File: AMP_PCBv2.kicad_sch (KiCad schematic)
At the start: 37 parts, among them J1 POWER, J2 EBRAKE, J3 MC, J4 STEERING, U1 Teensy4.0, U2 Adafruit_Feather_M0_RFM9x_LoR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, U2 Logo

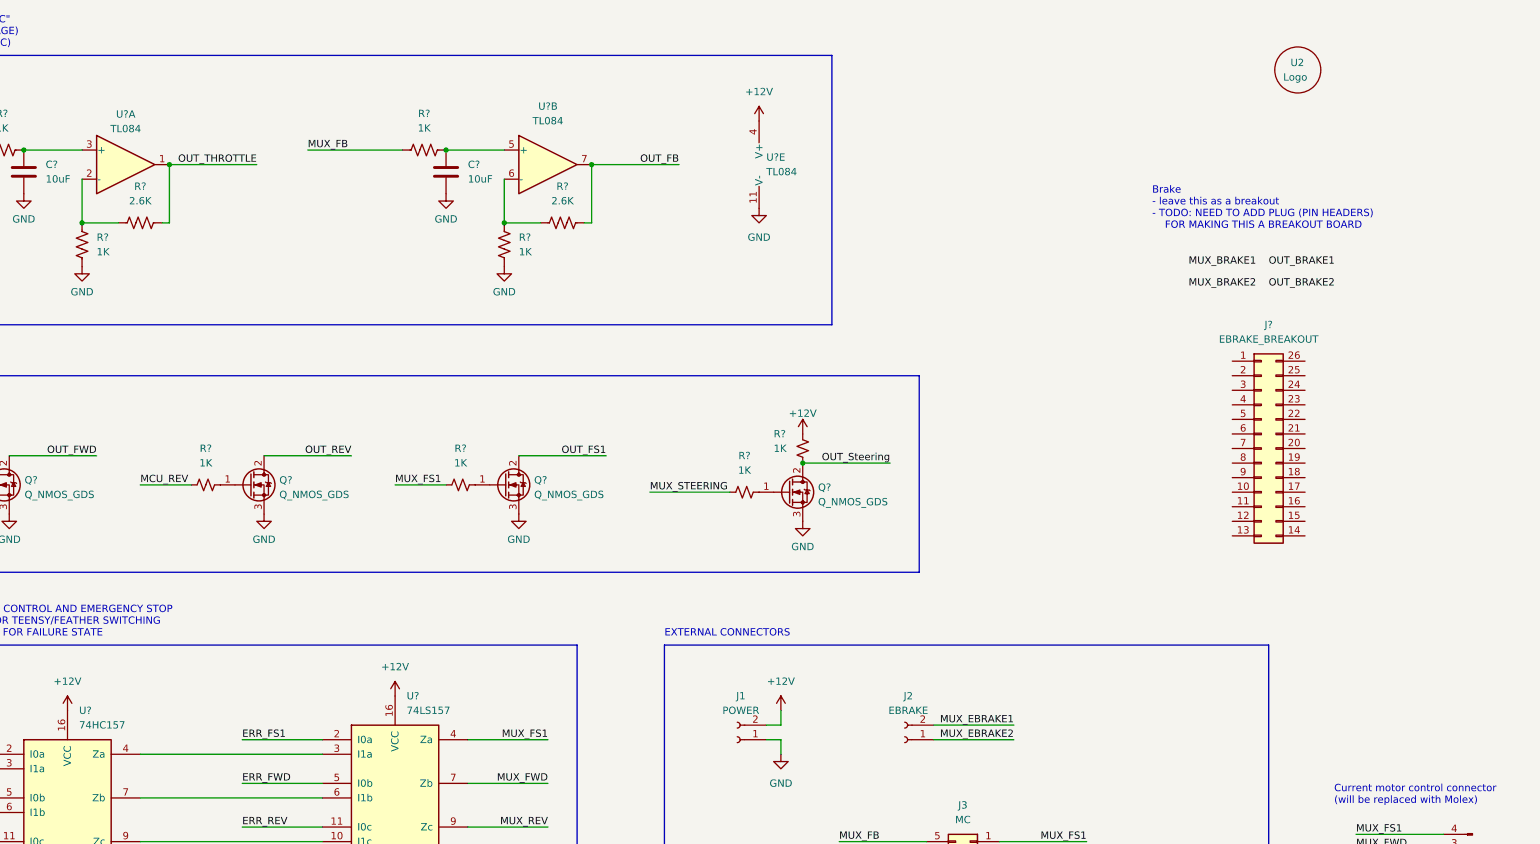
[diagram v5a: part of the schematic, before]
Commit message: Update op-amp PN and add e-brake breakout
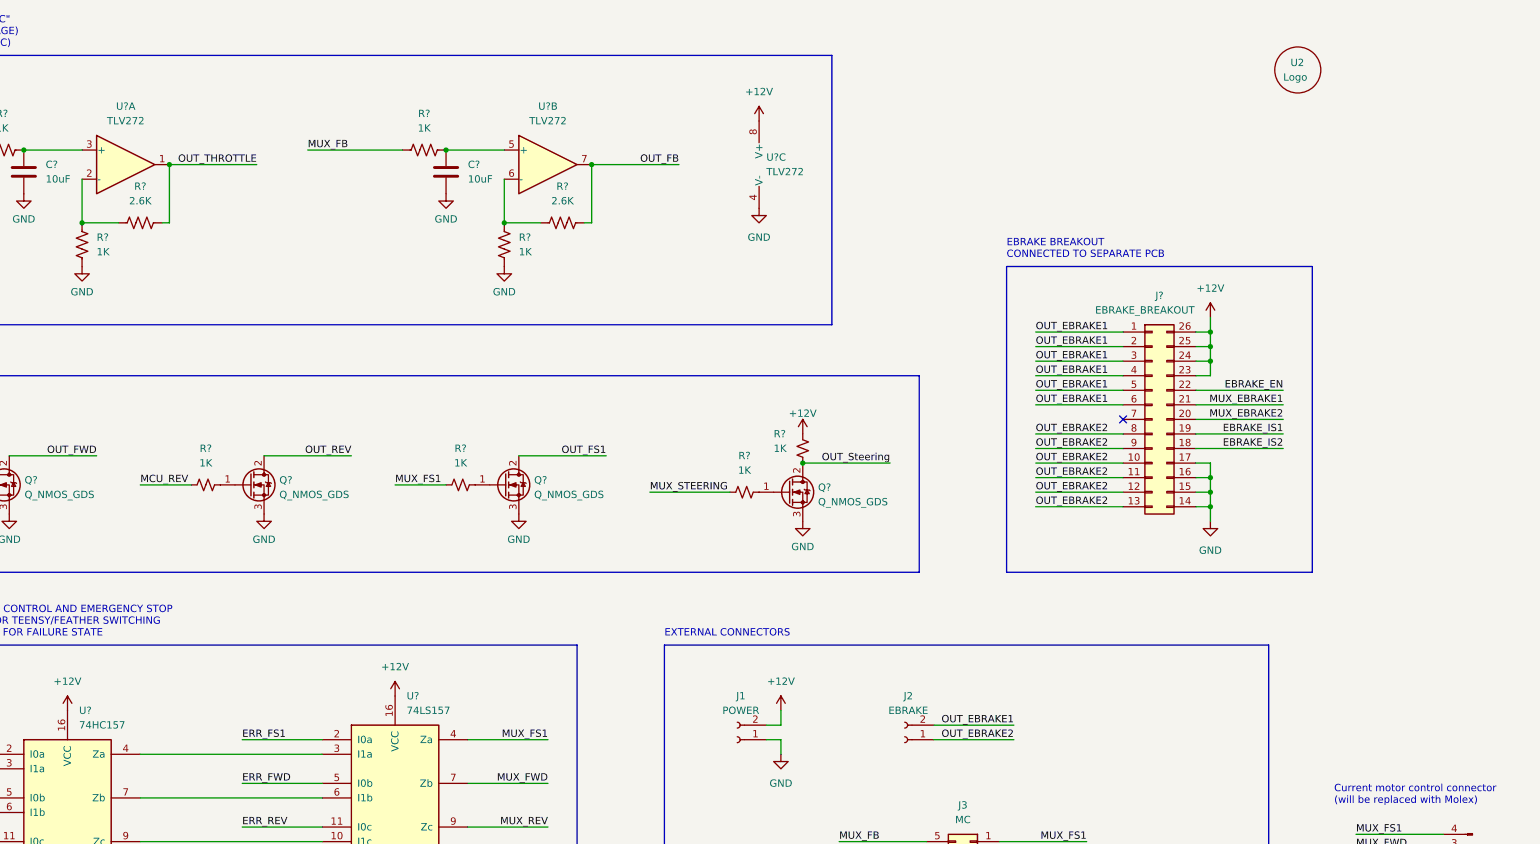
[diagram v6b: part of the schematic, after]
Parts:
- removed U? (x2): TL084, symbol Amplifier_Operational:TL084
- removed U?: TL084, Package_DIP:DIP-14_W7.62mm, symbol Amplifier_Operational:TL084
- added U? (x3): TLV272, symbol Amplifier_Operational:TLV2372
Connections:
- net +12V: now also J?.23 (Pin_23), J?.24 (Pin_24), J?.25 (Pin_25), J?.26 (Pin_26), U?.8 (V+)
- net GND: now also J?.14 (Pin_14), J?.15 (Pin_15), J?.16 (Pin_16), J?.17 (Pin_17), U?.4 (V-)
- net MUX_EBRAKE1: now also J?.21 (Pin_21); no longer J2.2 (Pin_2)
- net MUX_EBRAKE2: now also J?.20 (Pin_20); no longer J2.1 (Pin_1)
- net OUT_FB: now also U?.7
- net OUT_THROTTLE: now also U?.1
- net at R?.1, R?.1: now also U?.6 (-)
- net at R?.1, R?.1: now also U?.2 (-)
- net at C?.1, R?.2: now also U?.3 (+)
- net at C?.1, R?.2: now also U?.5 (+)
- net OUT_EBRAKE1: now reaches J?.1 (Pin_1)
- net OUT_EBRAKE1: now also J2.2 (Pin_2), J?.2 (Pin_2), J?.3 (Pin_3), J?.4 (Pin_4), J?.5 (Pin_5), J?.6 (Pin_6)
- net OUT_EBRAKE2: now reaches J?.10 (Pin_10)
- net OUT_EBRAKE2: now also J2.1 (Pin_1), J?.11 (Pin_11), J?.12 (Pin_12), J?.13 (Pin_13), J?.8 (Pin_8), J?.9 (Pin_9)
- net EBRAKE_IS2: now reaches J?.18 (Pin_18)
- net EBRAKE_IS1: now reaches J?.19 (Pin_19)
- net EBRAKE_EN: now reaches J?.22 (Pin_22)
- no-connect marks 3 -> 4
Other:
- note added: "EBRAKE BREAKOUT CONNECTED TO SEPARATE PCB"
- note removed: "Brake - leave this as a breakout - TODO: NEED TO ADD PLUG (PIN HEADERS) FOR MAKING THIS A BREAKOUT BOARD"
- moved on the sheet: J?

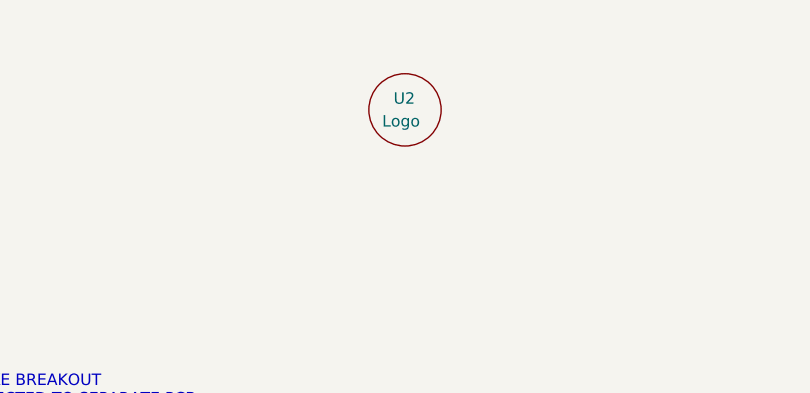
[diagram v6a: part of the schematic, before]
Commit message: Remove logo schematic designator
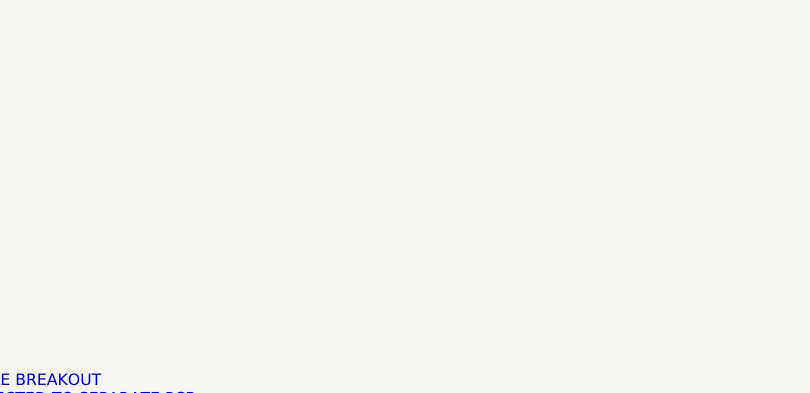
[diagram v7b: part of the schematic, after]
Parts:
- removed U2: Logo, AMP:Logo, symbol AMP:Logo
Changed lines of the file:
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@@
     (pin "1")
-  )
-  (symbol (lib_id "AMP:Logo") (at 361.95 26.67 0) (unit 1)
-    (in_bom no) (on_board yes)
-    (property "Reference" "U2" (id 0) (at 360.68 25.4 0)
-      (effects (font (size 1.27 1.27)) (justify left))
-    )
-    (property "Value" "Logo" (id 1) (at 359.41 27.94 0)
-      (effects (font (size 1.27 1.27)) (justify left))
-    )
-    (property "Footprint" "AMP:Logo" (id 2) (at 361.95 26.67 0)
-      (effects (font (size 1.27 1.27)) hide)
-    )
-    (property "Datasheet" "" (id 3) (at 361.95 26.67 0)
-      (effects (font (size 1.27 1.27)) hide)
-    )
   )
   (symbol (lib_id "power:GND") (at 191.77 245.11 0) (unit 1)
@@
       (reference "U1") (unit 1) (value "Teensy4.0") (footprint "teensy:Teensy40")
     )
-    (path "/83d62449-4592-47d6-9b07-6cbdf8842ef4"
-      (reference "U2") (unit 1) (value "Logo") (footprint "AMP:Logo")
-    )
     (path "/95fe3d96-e8a5-4077-a1d2-b0c02a43836e"

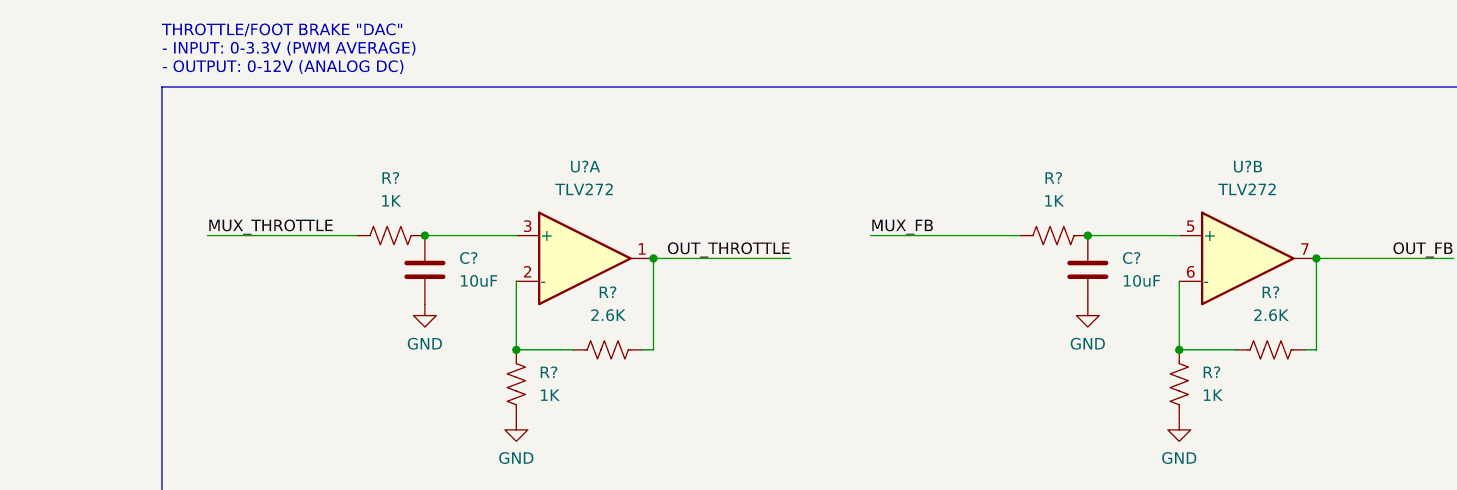
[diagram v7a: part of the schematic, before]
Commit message: Change DAC op-amp gain
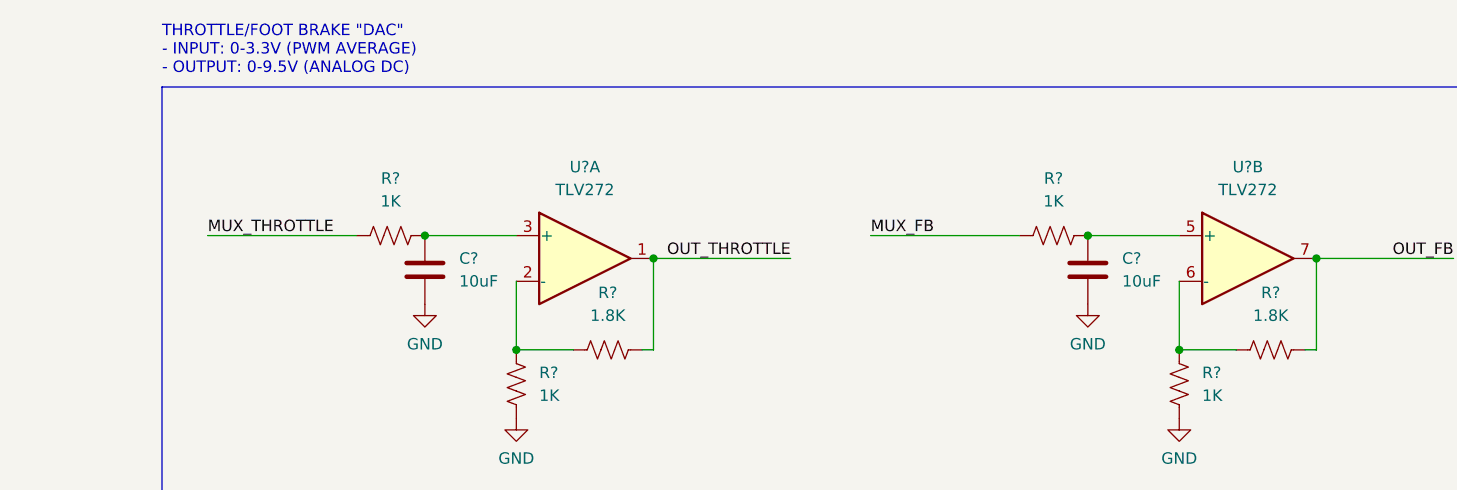
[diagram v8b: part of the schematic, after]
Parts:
- R? (x2): value 2.6K -> 1.8K
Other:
- note added: "THROTTLE/FOOT BRAKE "DAC" - INPUT: 0-3.3V (PWM AVERAGE) - OUTPUT: 0-9.5V (ANALOG DC)"
- note removed: "THROTTLE/FOOT BRAKE "DAC" - INPUT: 0-3.3V (PWM AVERAGE) - OUTPUT: 0-12V (ANALOG DC)"
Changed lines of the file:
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@@
     (effects (font (size 1.27 1.27)) (justify left bottom))
   )
-  (text "THROTTLE/FOOT BRAKE \"DAC\"\n- INPUT: 0-3.3V (PWM AVERAGE)\n- OUTPUT: 0-12V (ANALOG DC)"
+  (text "THROTTLE/FOOT BRAKE \"DAC\"\n- INPUT: 0-3.3V (PWM AVERAGE)\n- OUTPUT: 0-9.5V (ANALOG DC)"
     (at 110.49 22.86 0)
     (effects (font (size 1.27 1.27)) (justify left bottom))
@@
     (in_bom yes) (on_board yes) (fields_autoplaced)
     (property "Reference" "R?" (id 0) (at 233.68 46.99 90))
-    (property "Value" "2.6K" (id 1) (at 233.68 49.53 90))
+    (property "Value" "1.8K" (id 1) (at 233.68 49.53 90))
     (property "Footprint" "" (id 2) (at 233.934 52.324 90)
       (effects (font (size 1.27 1.27)) hide)
@@
     (in_bom yes) (on_board yes) (fields_autoplaced)
     (property "Reference" "R?" (id 0) (at 160.02 46.99 90))
-    (property "Value" "2.6K" (id 1) (at 160.02 49.53 90))
+    (property "Value" "1.8K" (id 1) (at 160.02 49.53 90))
     (property "Footprint" "" (id 2) (at 160.274 52.324 90)
       (effects (font (size 1.27 1.27)) hide)
@@
     )
     (path "/0984d1a3-dac9-4895-b89c-945999a5a91c"
-      (reference "R?") (unit 1) (value "2.6K") (footprint "")
+      (reference "R?") (unit 1) (value "1.8K") (footprint "")
     )
     (path "/2f8c9adc-797e-47d5-91d2-557a72ce1c9f"
@@
     )
     (path "/d5e0a62e-1109-48e3-a1f2-c93520d6a752"
-      (reference "R?") (unit 1) (value "2.6K") (footprint "")
+      (reference "R?") (unit 1) (value "1.8K") (footprint "")
     )
     (path "/d964fe63-e92a-4d3d-a690-b7b381ecd640"
